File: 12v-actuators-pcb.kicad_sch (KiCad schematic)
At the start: 9 parts, among them J2 3.5mm WR-TBL, J3 690367280676, J5 USB_B_Mini, J8 CAN, U1 MCP2551-I-SN

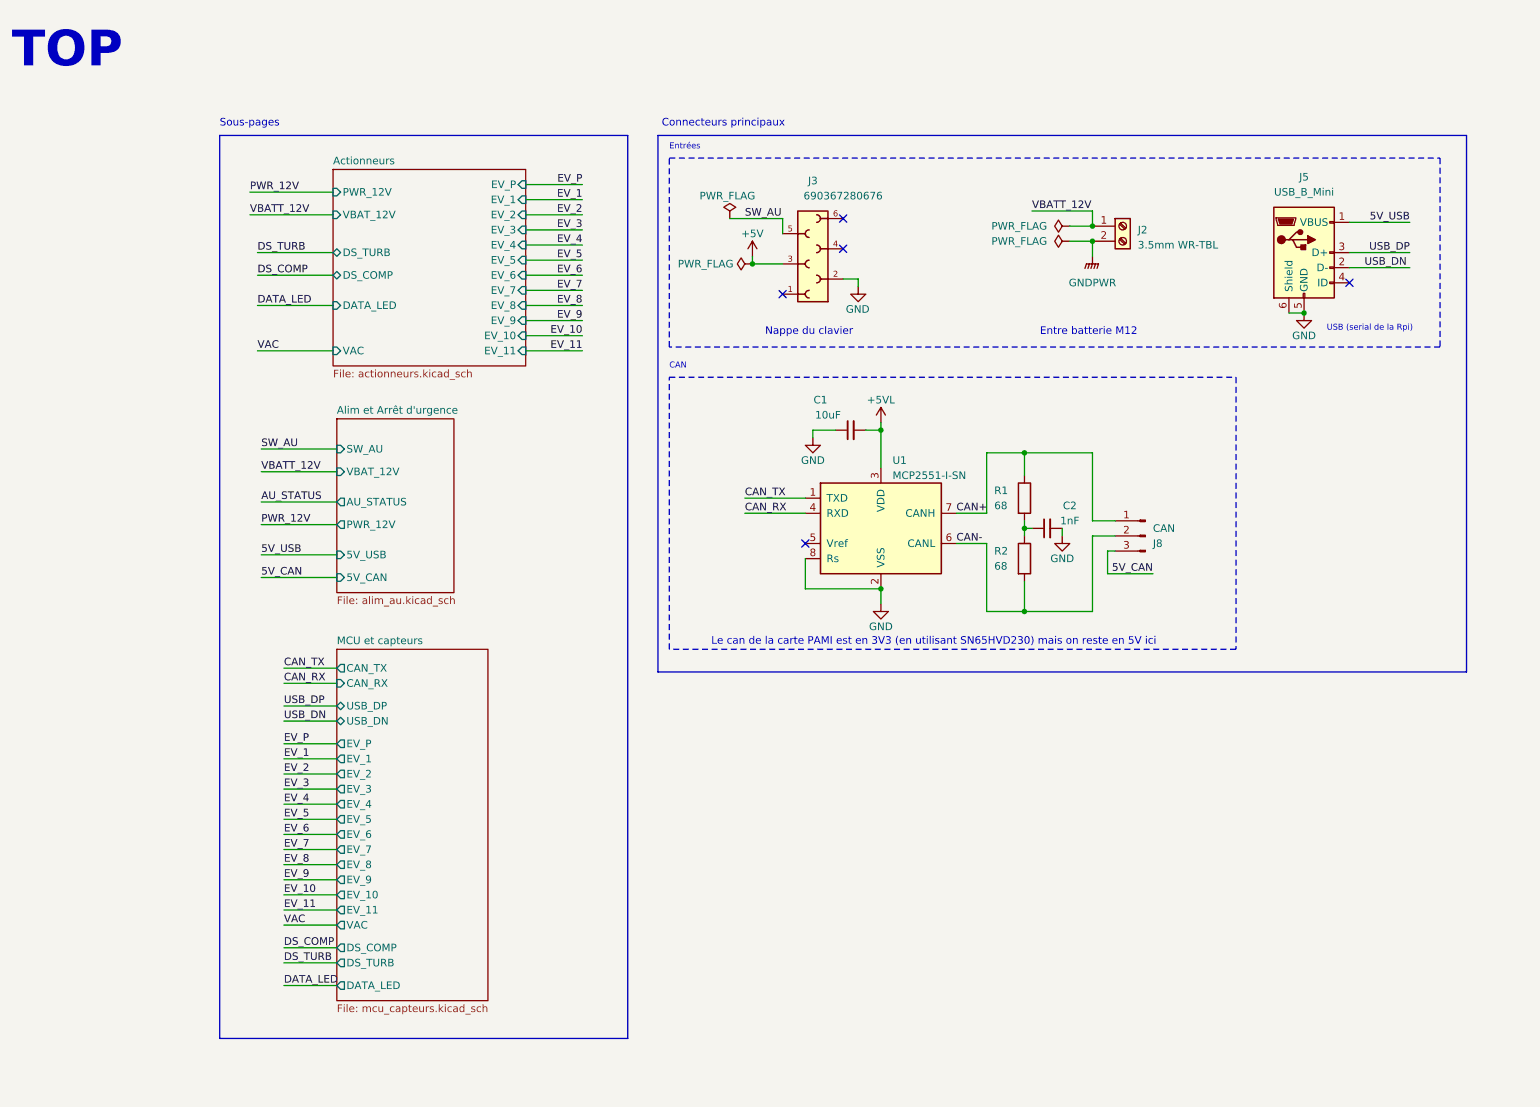
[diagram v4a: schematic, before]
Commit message: Correction de signaux non connectes, ajout de connecteur manquant, mise en forme du TOP
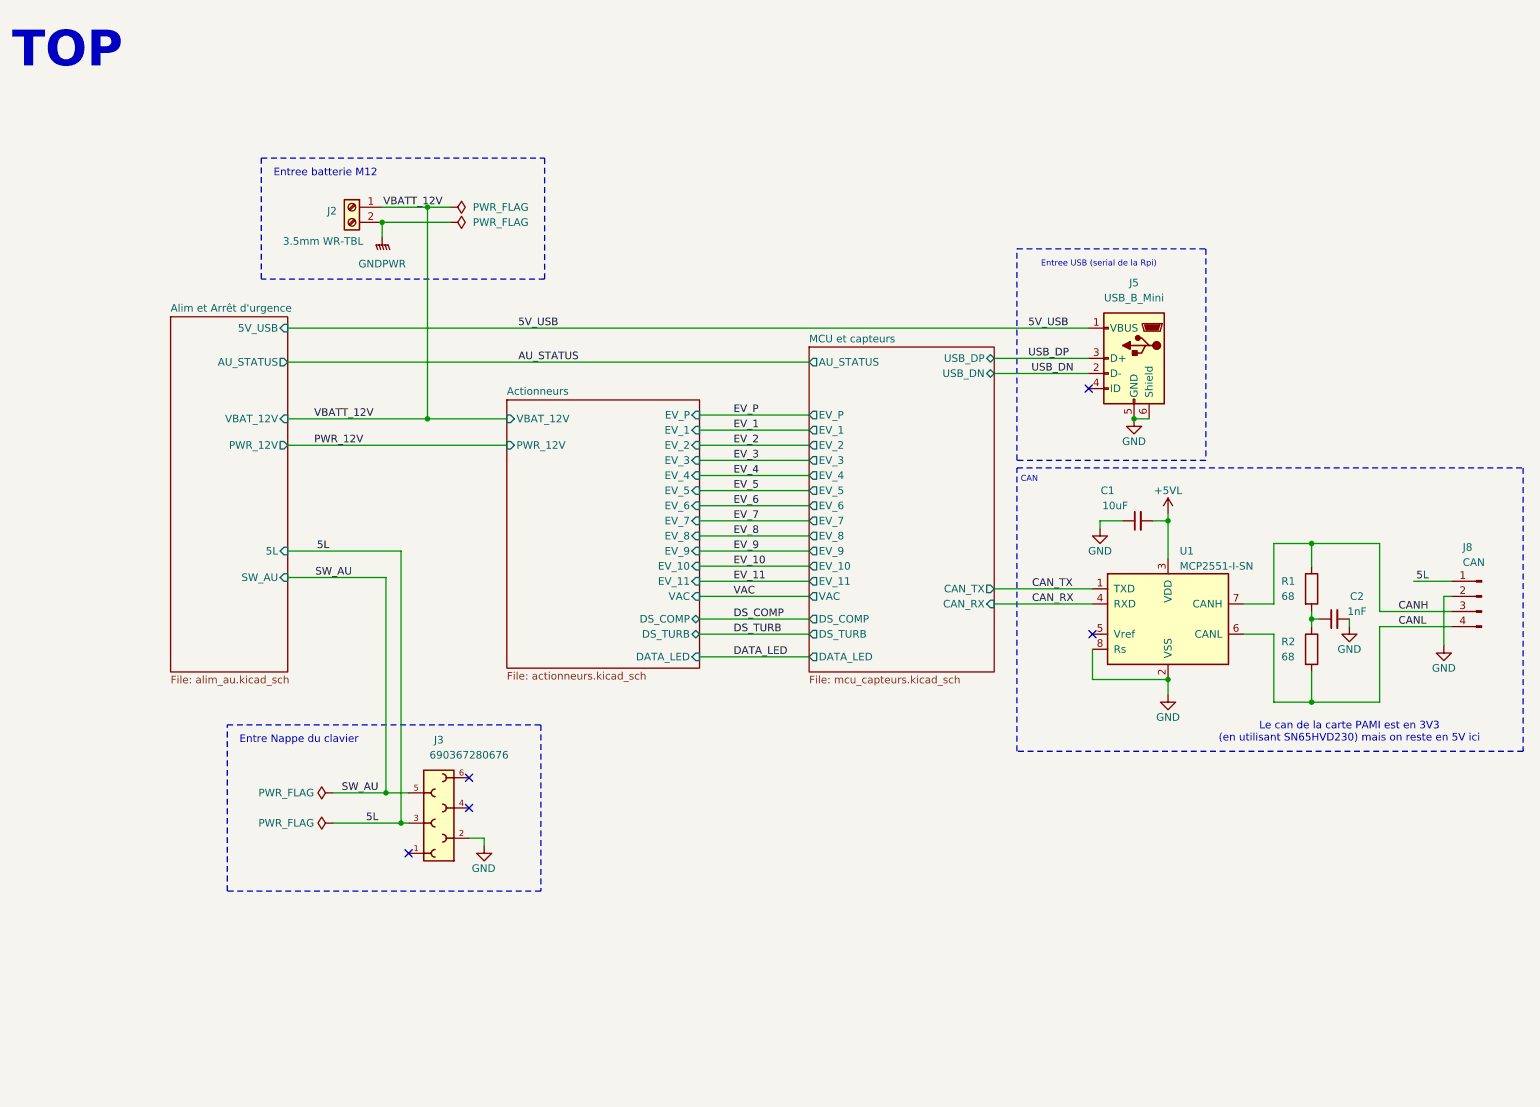
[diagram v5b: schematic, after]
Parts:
- J8: footprint Connector_PinHeader_2.54mm:PinHeader_1x03_P2.54mm_Vertical -> Connector_PinHeader_2.54mm:PinHeader_1x04_P2.54mm_Vertical; symbol Connector:Conn_01x03_Pin -> Connector:Conn_01x04_Pin
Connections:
- net GND: now also J8.2 (Pin_2)
- net +5V renamed 5L
- net 5L: now also J8.1 (Pin_1)
- net 5V_CAN renamed CANH
- net CANH: now also R1.1, U1.7 (CANH)
- removed net CAN+: J8.1 (Pin_1), R1.1, U1.7 (CANH)
- net CAN- renamed CANL
- net CANL: now also J8.4 (Pin_4); no longer J8.2 (Pin_2)
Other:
- sheet Alim et Arrêt d'urgence ports: added 5L; removed 5V_CAN
- sheet MCU et capteurs ports: added AU_STATUS; removed none
- note added: "Entre Nappe du clavier"
- note added: "Entree USB (serial de la Rpi)"
- note added: "Entree batterie M12"
- note removed: "Connecteurs principaux"
- note removed: "Entre batterie M12"
- note removed: "Entrées"
- note removed: "Nappe du clavier"
- note removed: "Sous-pages"
- note removed: "USB (serial de la Rpi)"
- moved on the sheet: C1, C2, J2, J3, J5, R1, R2, U1

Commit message: split des cartes
Todo: sync routage et ajout trou de fixation
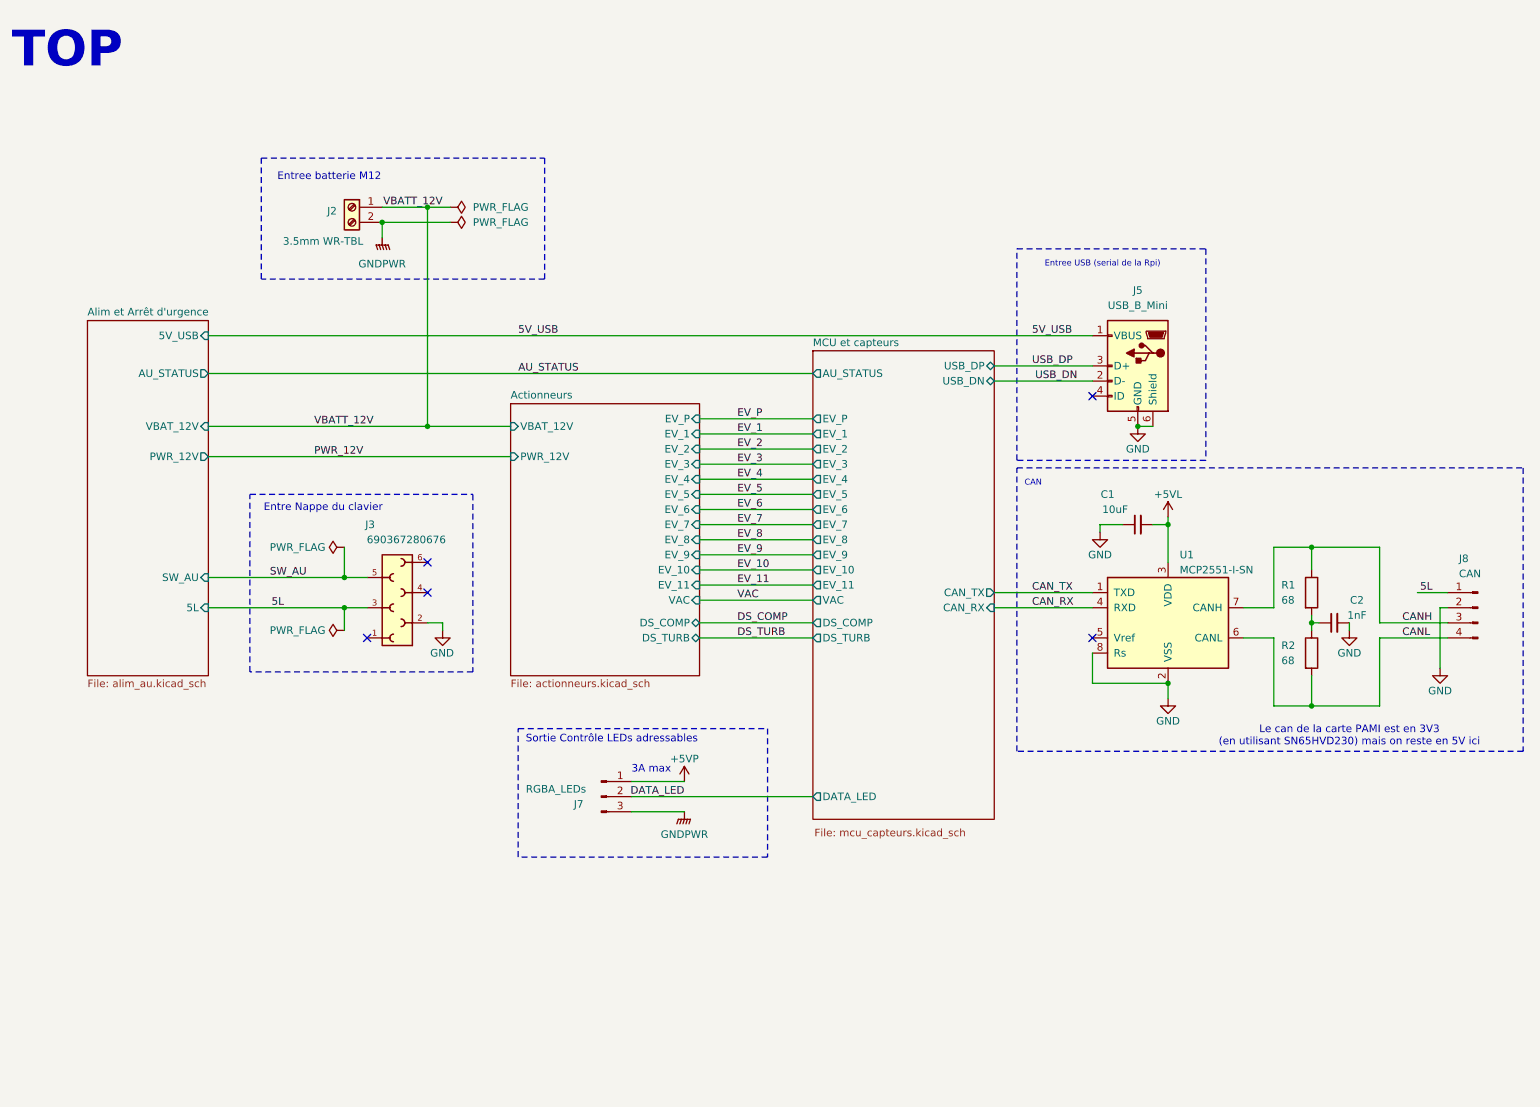
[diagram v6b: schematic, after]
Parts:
- added J7: RGBA_LEDs, Connector_PinHeader_2.54mm:PinHeader_1x03_P2.54mm_Vertical, symbol Connector:Conn_01x03_Pin
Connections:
- net DATA_LED: now also J7.2 (Pin_2)
- net GNDPWR: now also J7.3 (Pin_3)
- new net +5VP: J7.1 (Pin_1)
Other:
- sheet Actionneurs ports: added none; removed DATA_LED
- note added: "3A max"
- note added: "Sortie Contrôle LEDs adressables"
- moved on the sheet: C1, C2, J3, J5, J8, R1, R2, U1

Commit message: optimisation empreinte passif (TODO fp diode), TODO ajouter LED temoin diverse, groupement sur PCB des nouveaux composant
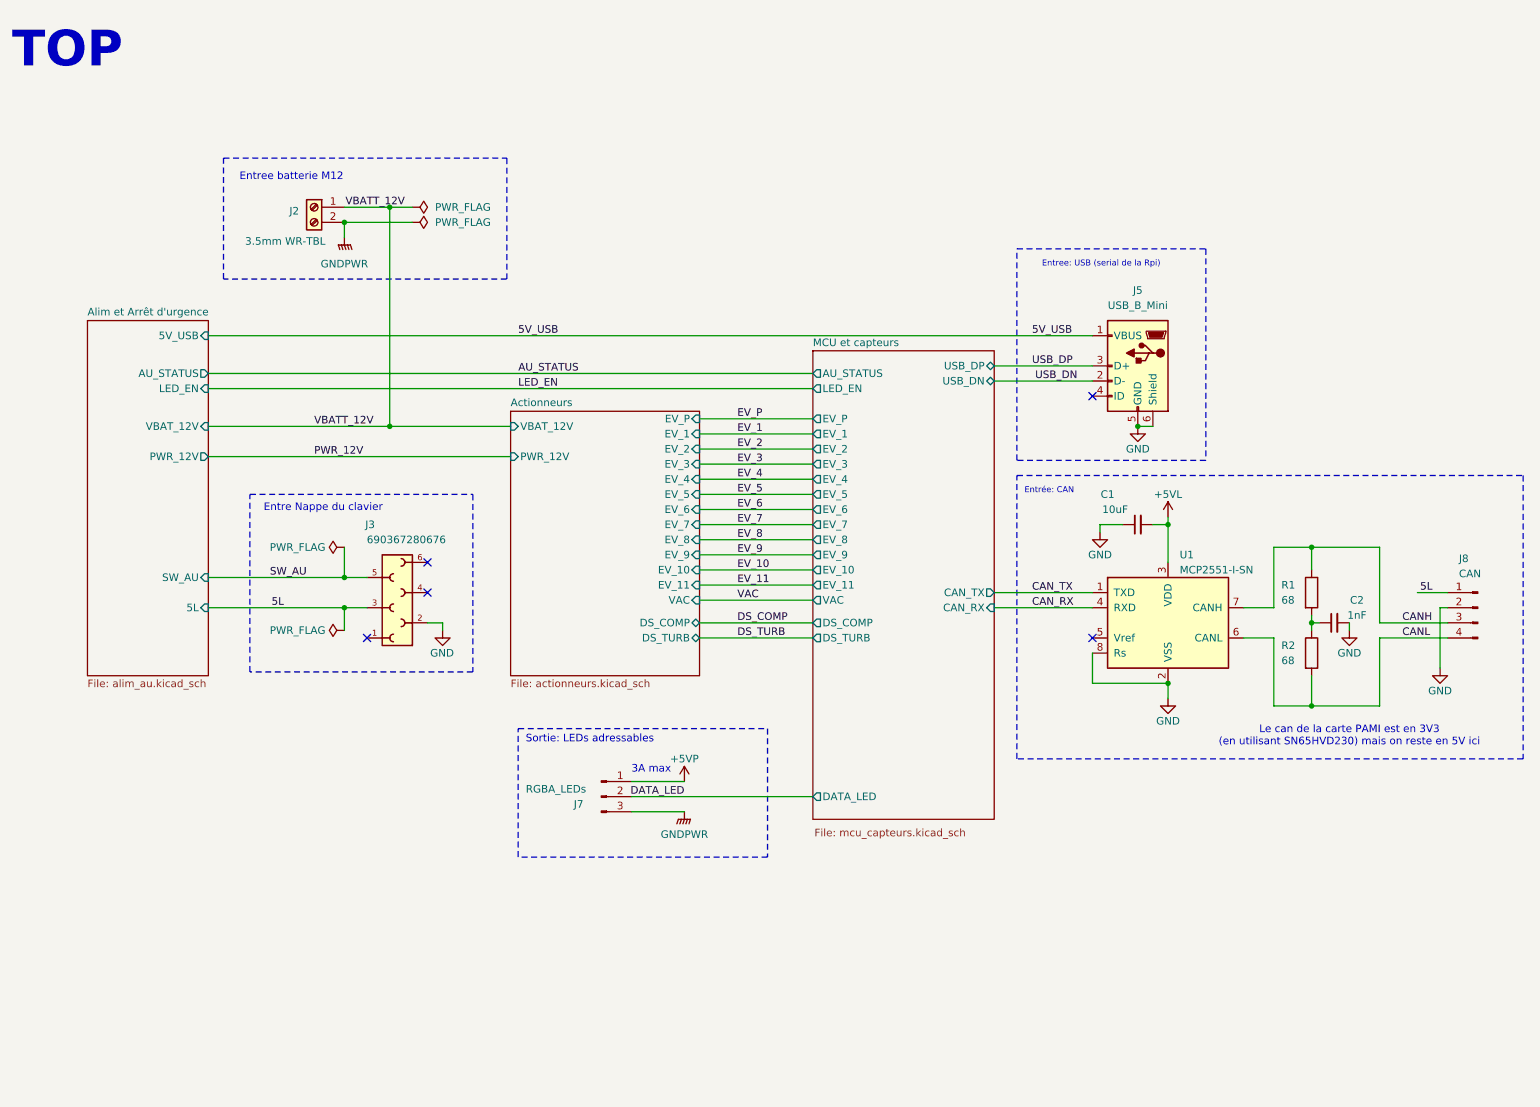
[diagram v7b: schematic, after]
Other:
- sheet Alim et Arrêt d'urgence ports: added LED_EN; removed none
- sheet MCU et capteurs ports: added LED_EN; removed none
- note added: "Entree: USB (serial de la Rpi)"
- note added: "Entrée: CAN"
- note added: "Sortie: LEDs adressables"
- note removed: "CAN"
- note removed: "Entree USB (serial de la Rpi)"
- note removed: "Sortie Contrôle LEDs adressables"
- moved on the sheet: J2
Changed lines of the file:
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@@
 	)
 	(junction
-		(at 83.82 82.55)
+		(at 77.47 82.55)
 		(diameter 0)
 		(color 0 0 0 0)
 	)
 	(junction
-		(at 76.2 48.26)
+		(at 69.85 48.26)
 		(diameter 0)
 		(color 0 0 0 0)
@@
 	)
 	(junction
-		(at 83.82 45.72)
+		(at 77.47 45.72)
 		(diameter 0)
 		(color 0 0 0 0)
@@
 	(wire
 		(pts
-			(xy 83.82 82.55) (xy 97.79 82.55)
-		)
-		(stroke
-			(width 0.5)
-			(type default)
-			(color 255 0 0 1)
-		)
-	)
-	(wire
-		(pts
 			(xy 232.41 114.3) (xy 232.41 115.57)
 		)
@@
 	(wire
 		(pts
-			(xy 76.2 48.26) (xy 76.2 50.8)
+			(xy 69.85 48.26) (xy 69.85 50.8)
 		)
 		(stroke
@@
 	(wire
 		(pts
+			(xy 77.47 82.55) (xy 97.79 82.55)
+		)
+		(stroke
+			(width 0.5)
+			(type default)
+			(color 255 0 0 1)
+		)
+	)
+	(wire
+		(pts
 			(xy 205.74 82.55) (xy 203.2 82.55)
 		)
@@
 	(wire
 		(pts
-			(xy 83.82 45.72) (xy 83.82 82.55)
+			(xy 77.47 45.72) (xy 77.47 82.55)
 		)
 		(stroke
@@
 	(wire
 		(pts
-			(xy 83.82 45.72) (xy 87.63 45.72)
+			(xy 77.47 45.72) (xy 81.28 45.72)
 		)
 		(stroke
@@
 	(wire
 		(pts
-			(xy 87.63 48.26) (xy 76.2 48.26)
+			(xy 81.28 48.26) (xy 69.85 48.26)
 		)
 		(stroke
@@
 	(wire
 		(pts
-			(xy 46.99 82.55) (xy 83.82 82.55)
+			(xy 46.99 82.55) (xy 77.47 82.55)
 		)
 		(stroke
@@
 	(wire
 		(pts
+			(xy 46.99 76.2) (xy 148.59 76.2)
+		)
+		(stroke
+			(width 0)
+			(type default)
+		)
+	)
+	(wire
+		(pts
 			(xy 69.85 113.03) (xy 73.66 113.03)
 		)
@@
 	(wire
 		(pts
-			(xy 76.2 45.72) (xy 83.82 45.72)
+			(xy 69.85 45.72) (xy 77.47 45.72)
 		)
 		(stroke
@@
 	)
 	(rectangle
-		(start 182.88 89.535)
-		(end 267.97 137.16)
+		(start 182.88 90.805)
+		(end 267.97 138.43)
 		(stroke
 			(width 0)
@@
 	)
 	(rectangle
-		(start 55.88 37.465)
-		(end 103.505 57.785)
+		(start 49.53 37.465)
+		(end 97.155 57.785)
 		(stroke
 			(width 0)
@@
 		)
 	)
-	(text "Sortie Contrôle LEDs adressables"
+	(text "Sortie: LEDs adressables"
 		(exclude_from_sim no)
 		(at 100.33 135.89 0)
@@
 		)
 	)
-	(text "CAN"
+	(text "Entrée: CAN"
 		(exclude_from_sim no)
-		(at 184.15 92.71 0)
+		(at 184.15 93.98 0)
 		(effects
 			(font
@@
 	(text "Entree batterie M12"
 		(exclude_from_sim no)
-		(at 67.31 40.64 0)
+		(at 60.96 40.64 0)
 		(effects
 			(font
@@
 		)
 	)
-	(text "Entree USB (serial de la Rpi)"
+	(text "Entree: USB (serial de la Rpi)"
 		(exclude_from_sim no)
 		(at 207.01 55.88 0)
@@
 	)
 	(label "VBATT_12V"
-		(at 86.36 45.72 180)
+		(at 80.01 45.72 180)
 		(effects
 			(font
@@
 		)
 	)
+	(label "LED_EN"
+		(at 99.06 76.2 0)
+		(effects
+			(font
+				(size 1.27 1.27)
+			)
+			(justify left bottom)
+		)
+	)
 	(label "5V_USB"
 		(at 99.06 67.31 0)
@@
 	(symbol
 		(lib_id "Connector:Screw_Terminal_01x02")
-		(at 71.12 45.72 0)
+		(at 64.77 45.72 0)
 		(mirror y)
 		(unit 1)
@@
 		(dnp no)
 		(property "Reference" "J2"
-			(at 68.58 46.355 0)
+			(at 62.23 46.355 0)
 			(effects
 				(font
@@
 		)
 		(property "Value" "3.5mm WR-TBL"
-			(at 73.025 51.435 0)
+			(at 66.675 51.435 0)
 			(effects
 				(font
@@
 		)
 		(property "Footprint" "ConnectorsEvo:691321100002"
-			(at 71.12 45.72 0)
+			(at 64.77 45.72 0)
 			(effects
 				(font
@@
 		)
 		(property "Datasheet" "~"
-			(at 71.12 45.72 0)
+			(at 64.77 45.72 0)
 			(effects
 				(font
@@
 		)
 		(property "Description" ""
-			(at 71.12 45.72 0)
+			(at 64.77 45.72 0)
 			(effects
 				(font
@@
 	(symbol
 		(lib_id "power:PWR_FLAG")
-		(at 87.63 48.26 270)
+		(at 81.28 48.26 270)
 		(mirror x)
 		(unit 1)
@@
 		(dnp no)
 		(property "Reference" "#FLG03"
-			(at 89.535 48.26 0)
+			(at 83.185 48.26 0)
 			(effects
 				(font
@@
 		)
 		(property "Value" "PWR_FLAG"
-			(at 91.44 48.26 90)
+			(at 85.09 48.26 90)
 			(effects
 				(font
@@
 		)
 		(property "Footprint" ""
-			(at 87.63 48.26 0)
+			(at 81.28 48.26 0)
 			(effects
 				(font
@@
 		)
 		(property "Datasheet" "~"
-			(at 87.63 48.26 0)
+			(at 81.28 48.26 0)
 			(effects
 				(font
@@
 		)
 		(property "Description" ""
-			(at 87.63 48.26 0)
+			(at 81.28 48.26 0)
 			(effects
 				(font
@@
 	(symbol
 		(lib_id "power:GNDPWR")
-		(at 76.2 50.8 0)
+		(at 69.85 50.8 0)
 		(mirror y)
 		(unit 1)
@@
 		(dnp no)
 		(property "Reference" "#PWR03"
-			(at 76.2 55.88 0)
+			(at 69.85 55.88 0)
 			(effects
 				(font
@@
 		)
 		(property "Value" "GNDPWR"
-			(at 76.2 55.245 0)
+			(at 69.85 55.245 0)
 			(effects
 				(font
@@
 		)
 		(property "Footprint" ""
-			(at 76.2 52.07 0)
+			(at 69.85 52.07 0)
 			(effects
 				(font
@@
 		)
 		(property "Datasheet" ""
-			(at 76.2 52.07 0)
+			(at 69.85 52.07 0)
 			(effects
 				(font
@@
 		)
 		(property "Description" ""
-			(at 76.2 50.8 0)
+			(at 69.85 50.8 0)
 			(effects
 				(font
@@
 	(symbol
 		(lib_id "power:PWR_FLAG")
-		(at 87.63 45.72 270)
+		(at 81.28 45.72 270)
 		(mirror x)
 		(unit 1)
@@
 		(dnp no)
 		(property "Reference" "#FLG02"
-			(at 89.535 45.72 0)
+			(at 83.185 45.72 0)
 			(effects
 				(font
@@
 		)
 		(property "Value" "PWR_FLAG"
-			(at 91.44 45.72 90)
+			(at 85.09 45.72 90)
 			(effects
 				(font
@@
 		)
 		(property "Footprint" ""
-			(at 87.63 45.72 0)
+			(at 81.28 45.72 0)
 			(effects
 				(font
@@
 		)
 		(property "Datasheet" "~"
-			(at 87.63 45.72 0)
+			(at 81.28 45.72 0)
 			(effects
 				(font
@@
 		)
 		(property "Description" ""
-			(at 87.63 45.72 0)
+			(at 81.28 45.72 0)
 			(effects
 				(font
@@
 	)
 	(sheet
-		(at 97.79 78.74)
-		(size 31.75 45.72)
+		(at 97.79 80.01)
+		(size 31.75 44.45)
 		(fields_autoplaced yes)
 		(stroke
@@
 		)
 		(property "Sheetname" "Actionneurs"
-			(at 97.79 78.0284 0)
+			(at 97.79 79.2984 0)
 			(effects
 				(font
@@
 			)
 		)
+		(pin "LED_EN" input
+			(at 46.99 76.2 0)
+			(effects
+				(font
+					(size 1.27 1.27)
+				)
+				(justify right)
+			)
+		)
 		(instances
 			(project "12v-actuators-pcb"
@@
 			(effects
 				(font
+					(size 1.27 1.27)
+				)
+				(justify left)
+			)
+		)
+		(pin "LED_EN" output
+			(at 148.59 76.2 180)
+			(effects
+				(font
